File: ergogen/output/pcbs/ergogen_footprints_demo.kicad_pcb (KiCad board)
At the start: 2 copper layers, 230 x 95 mm, 112 parts

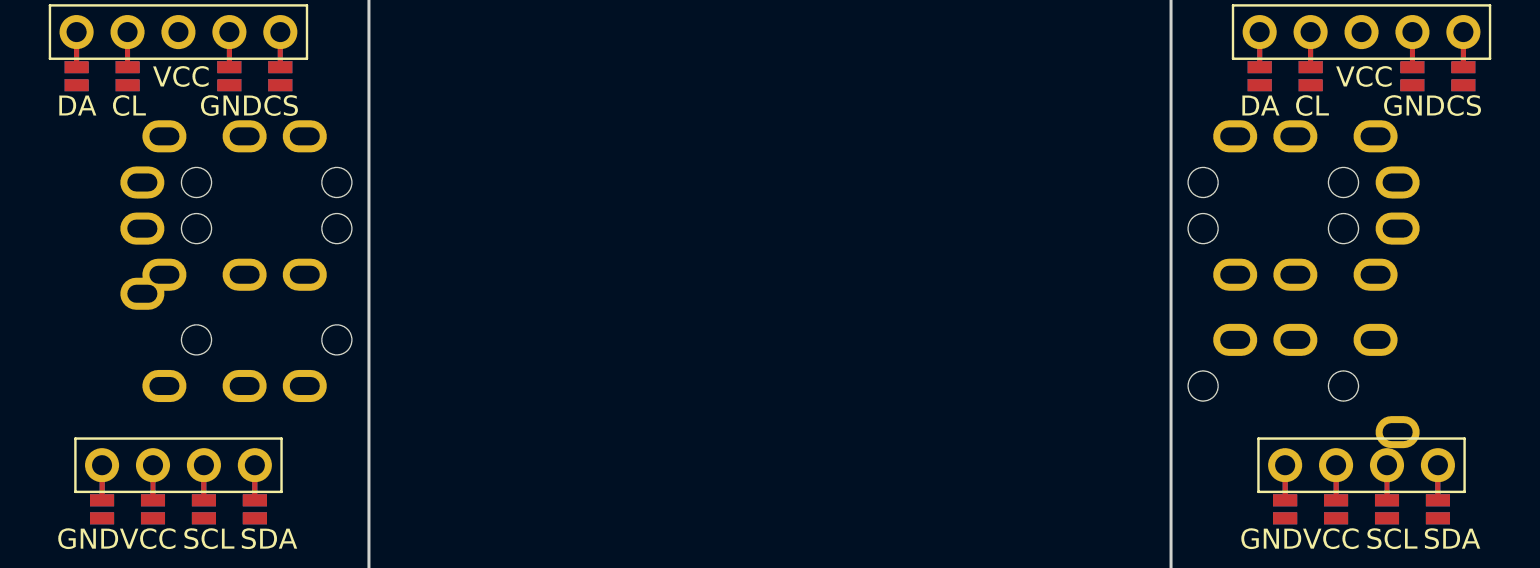
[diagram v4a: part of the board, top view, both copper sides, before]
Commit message: Update TRRS footprint pinout and library
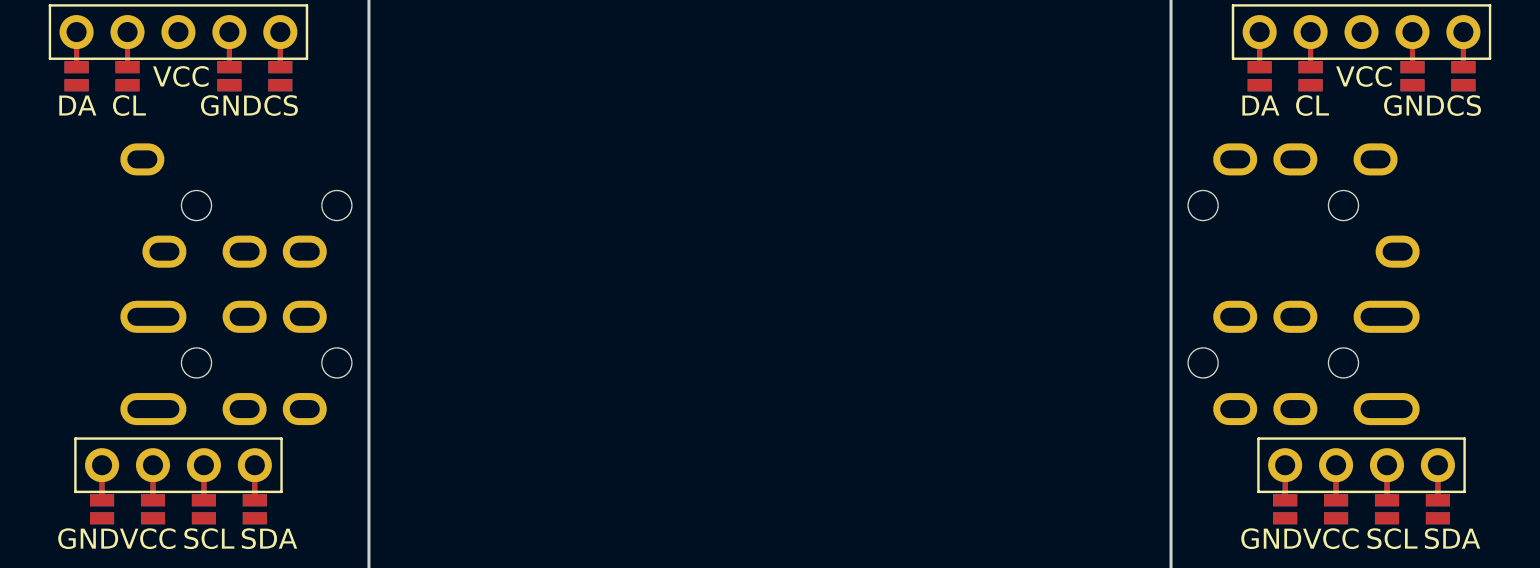
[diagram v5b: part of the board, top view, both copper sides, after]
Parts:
- TRRS1, TRRS2: footprint ceoloide:trrs_pj320a (reversible) -> ceoloide:trrs_pj320a
- TRRS3, TRRS4: footprint ceoloide:trrs_pj320a -> ceoloide:trrs_pj320a (reversible, symmetric)
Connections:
- TRRS1 pad 2: B -> GND
- TRRS1 pad 3: GND -> DAT
- TRRS2 pad 2: B -> GND
- TRRS2 pad 3: GND -> DAT
- TRRS3 pad 2: B -> GND
- TRRS3 pad 3: GND -> DAT
- TRRS4 pad 2: B -> GND
- TRRS4 pad 3: GND -> DAT

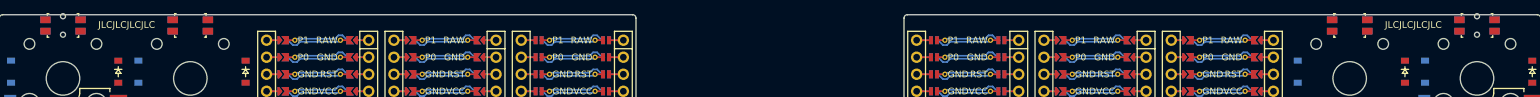
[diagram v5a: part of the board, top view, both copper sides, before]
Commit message: Update reset switch position
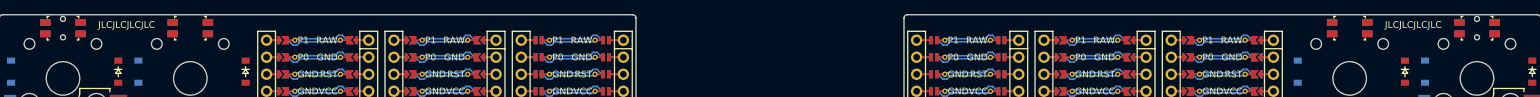
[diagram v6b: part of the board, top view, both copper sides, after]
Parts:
- moved RST1 0.40 mm to (81.0, 54.5)
- moved RST2 0.40 mm to (254.0, 54.5)
- moved RST3 0.40 mm to (62.0, 54.5)
- moved RST4 0.40 mm to (273.0, 54.5)
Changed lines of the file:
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@@
     )
         (module "ceoloide:reset_button_smd_side" (layer F.Cu)
-          (at 81 54.1 0)
+          (at 81 54.5 0)
           (attr smd)
           (fp_text value "reset_button_smd_side" (at 0 2.5 0) (layer F.Fab)
@@
       )
         (module "ceoloide:reset_button_smd_side" (layer F.Cu)
-          (at 254 54.1 0)
+          (at 254 54.5 0)
           (attr smd)
           (fp_text value "reset_button_smd_side" (at 0 2.5 0) (layer F.Fab)
@@
       )
         (module "ceoloide:reset_button_smd_side" (layer F.Cu)
-          (at 62 54.1 0)
+          (at 62 54.5 0)
           (attr smd)
           (fp_text value "reset_button_smd_side" (at 0 2.5 0) (layer F.Fab)
@@
       )
         (module "ceoloide:reset_button_smd_side" (layer F.Cu)
-          (at 273 54.1 0)
+          (at 273 54.5 0)
           (attr smd)
           (fp_text value "reset_button_smd_side" (at 0 2.5 0) (layer F.Fab)

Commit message: Update footprint library and reference for MCU / Display
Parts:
- DISP1, DISP2, DISP3, DISP4, DISP5, DISP6: footprint ceoloide:nice_view -> ceoloide:display_nice_view
- JST1, JST2: footprint ceoloide/battery_connector_jst_ph_2 -> ceoloide:battery_connector_jst_ph_2
- MCU1, MCU2, MCU3, MCU4, MCU5, MCU6: footprint ceoloide:nice_nano -> ceoloide:mcu_nice_nano

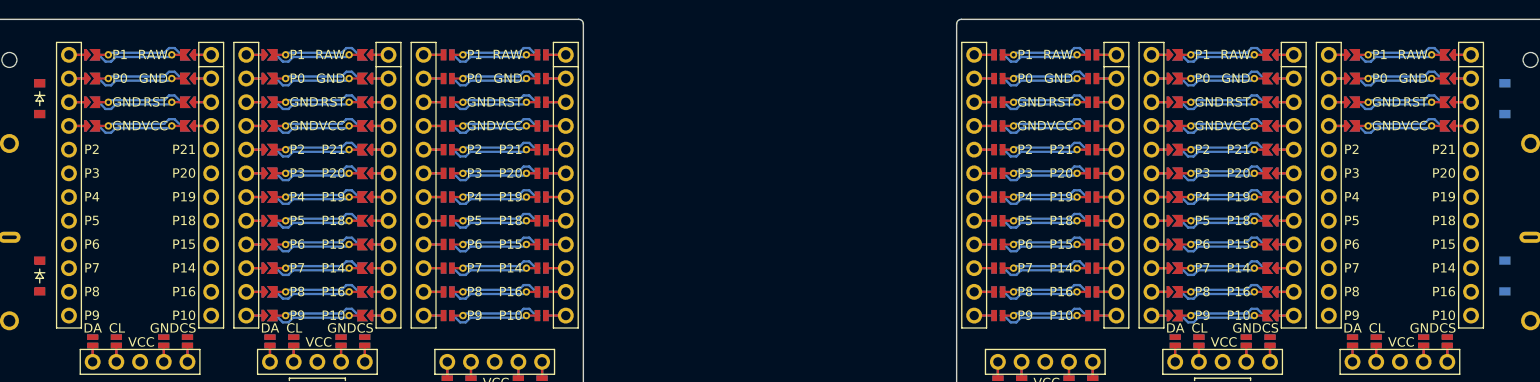
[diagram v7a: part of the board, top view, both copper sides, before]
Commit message: Update nice!nano footprint
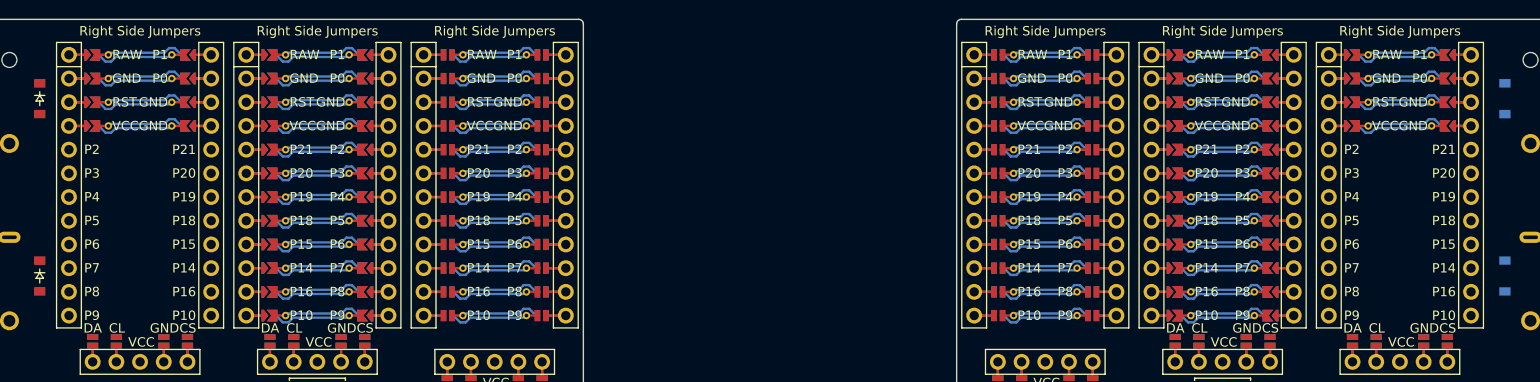
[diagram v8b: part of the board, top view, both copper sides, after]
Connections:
- MCU1 pad 1: RAW -> P1
- MCU1 pad 10: P14 -> P7
- MCU1 pad 11: P16 -> P8
- MCU1 pad 113: P9 -> P10
- MCU1 pad 114: P8 -> P16
- MCU1 pad 115: P7 -> P14
- MCU1 pad 116: P6 -> P15
- MCU1 pad 117: P5 -> P18
- MCU1 pad 118: P4 -> P19
- MCU1 pad 119: P3 -> P20
- MCU1 pad 12: P10 -> P9
- MCU1 pad 120: P2 -> P21
- MCU1 pad 121: GND -> VCC
- MCU1 pad 122: GND -> RST
- MCU1 pad 123: P0 -> GND
- MCU1 pad 124: P1 -> RAW
- MCU1 pad 2: GND -> P0
- MCU1 pad 3: RST -> GND
- MCU1 pad 4: VCC -> GND
- MCU1 pad 5: P21 -> P2
- MCU1 pad 6: P20 -> P3
- MCU1 pad 7: P19 -> P4
- MCU1 pad 8: P18 -> P5
- MCU1 pad 9: P15 -> P6
- MCU2 pad 1: RAW -> P1
- MCU2 pad 10: P14 -> P7
- MCU2 pad 11: P16 -> P8
- MCU2 pad 113: P9 -> P10
- MCU2 pad 114: P8 -> P16
- MCU2 pad 115: P7 -> P14
- MCU2 pad 116: P6 -> P15
- MCU2 pad 117: P5 -> P18
- MCU2 pad 118: P4 -> P19
- MCU2 pad 119: P3 -> P20
- MCU2 pad 12: P10 -> P9
- MCU2 pad 120: P2 -> P21
- MCU2 pad 121: GND -> VCC
- MCU2 pad 122: GND -> RST
- MCU2 pad 123: P0 -> GND
- MCU2 pad 124: P1 -> RAW
- MCU2 pad 2: GND -> P0
- MCU2 pad 3: RST -> GND
- MCU2 pad 4: VCC -> GND
- MCU2 pad 5: P21 -> P2
- MCU2 pad 6: P20 -> P3
- MCU2 pad 7: P19 -> P4
- MCU2 pad 8: P18 -> P5
- MCU2 pad 9: P15 -> P6
- MCU3 pad 113: P9 -> P10
- MCU3 pad 114: P8 -> P16
- MCU3 pad 115: P7 -> P14
- MCU3 pad 116: P6 -> P15
- MCU3 pad 117: P5 -> P18
- MCU3 pad 118: P4 -> P19
- MCU3 pad 119: P3 -> P20
- MCU3 pad 120: P2 -> P21
- MCU3 pad 121: GND -> VCC
- MCU3 pad 122: GND -> RST
- MCU3 pad 123: P0 -> GND
- MCU3 pad 124: P1 -> RAW
- MCU4 pad 113: P9 -> P10
- MCU4 pad 114: P8 -> P16
- MCU4 pad 115: P7 -> P14
- MCU4 pad 116: P6 -> P15
- MCU4 pad 117: P5 -> P18
- MCU4 pad 118: P4 -> P19
- MCU4 pad 119: P3 -> P20
- MCU4 pad 120: P2 -> P21
- MCU4 pad 121: GND -> VCC
- MCU4 pad 122: GND -> RST
- MCU4 pad 123: P0 -> GND
- MCU4 pad 124: P1 -> RAW
- MCU5 pad 121: GND -> VCC
- MCU5 pad 122: GND -> RST
- MCU5 pad 123: P0 -> GND
- MCU5 pad 124: P1 -> RAW
- MCU6 pad 121: GND -> VCC
- MCU6 pad 122: GND -> RST
- MCU6 pad 123: P0 -> GND
- MCU6 pad 124: P1 -> RAW
